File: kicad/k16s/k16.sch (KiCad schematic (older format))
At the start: 352 parts, among them J1 PCIEPWR, J3 PINHD-1X4, J5 PINHD-1X4, Q1 NDS351AN, U1 AVALON, U10 AVALON, U11 AVALON, U12 AVALON, U13 AVALON, U14 AVALON, U15 AVALON, U16 AVALON, U17 PIC16LF1459, U18 IR3895, U19 IR3895, U2 AVALON, U20 MCP16321, U21 NL27WZ14, U22 AP7217D / RT9166A, U23 AP7217D / RT9166A, U24 74AUP2G02, U25 NL27WZ14, U3 AVALON, U4 AVALON, U5 AVALON, U6 AVALON, U7 AVALON, U8 AVALON, U9 AVALON, X1 ASMDB

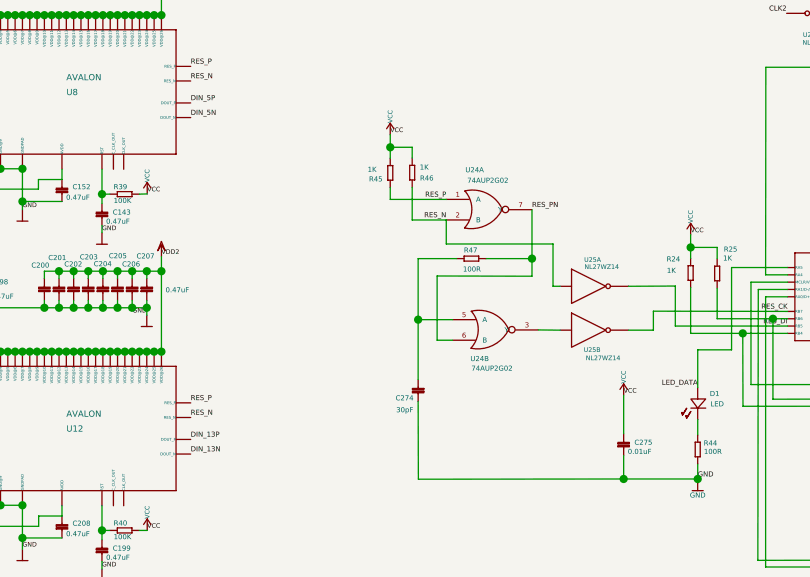
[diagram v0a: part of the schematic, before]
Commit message: Small tweaks to the K16
Fixed netlist packages, PCB and schematics values and updated BOM
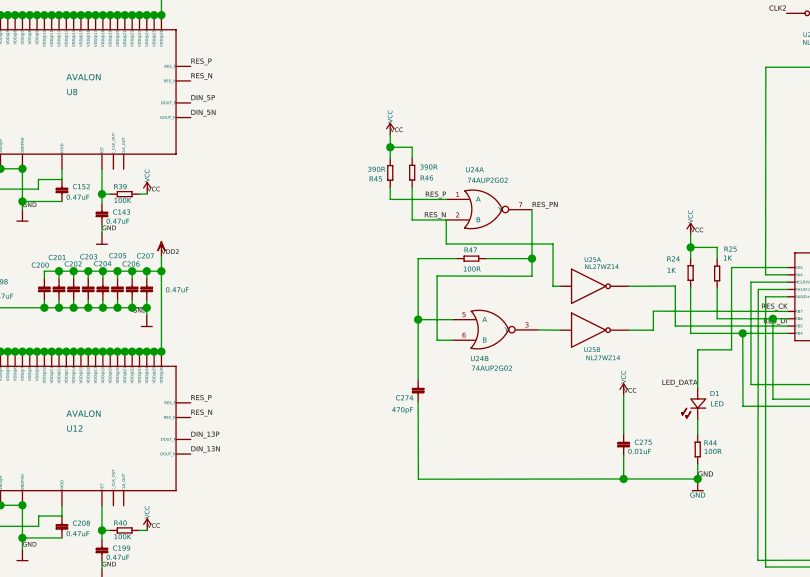
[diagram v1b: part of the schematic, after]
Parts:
- C274: value 30pF -> 470pF
- R45, R46: value 1K -> 390R
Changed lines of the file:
@@
-EESchema Schematic File Version 2  date Mon 12 Aug 2013 08:32:43 AM ICT
+EESchema Schematic File Version 2  date 24. 12. 2013 15:35:33
 LIBS:k16
 LIBS:power
@@
 LIBS:valves
 LIBS:k16-cache
-EELAYER 24 0
+EELAYER 27 0
 EELAYER END
 $Descr A3 16535 11693
@@
 Sheet 1 1
 Title "Klondike 16 ASIC Miner"
-Date "12 aug 2013"
-Rev ""
+Date "24 dec 2013"
+Rev "0.3.2"
 Comp ""
-Comment1 ""
+Comment1 "For 110nm Avalons - A256"
 Comment2 ""
 Comment3 ""
@@
 P 11857 6443
 F 0 "C274" H 11877 6447 22  0000 L BNN
-F 1 "30pF" H 11878 6499 22  0000 L BNN
+F 1 "470pF" H 11878 6499 22  0000 L BNN
 F 2 "" H 11857 6443 60  0001 C CNN
 F 3 "" H 11857 6443 60  0001 C CNN
@@
 P 11735 5475
 F 0 "R45" V 11775 5382 22  0000 L BNN
-F 1 "1K" V 11733 5376 22  0000 L BNN
+F 1 "390R" V 11733 5376 22  0000 L BNN
 F 2 "" H 11735 5475 60  0001 C CNN
 F 3 "" H 11735 5475 60  0001 C CNN
@@
 P 11831 5474
 F 0 "R46" V 11868 5508 22  0000 L BNN
-F 1 "1K" V 11820 5507 22  0000 L BNN
+F 1 "390R" V 11820 5507 22  0000 L BNN
 F 2 "" H 11831 5474 60  0001 C CNN
 F 3 "" H 11831 5474 60  0001 C CNN
